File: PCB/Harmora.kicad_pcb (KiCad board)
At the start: 2 copper layers, 287 x 138 mm, 192 parts, among them J1 USBC, J4 JST-EH, J5 128x64 2.42 inc, P1 10k, P2 10k, P3 10k, P4 10k, U1 SS49E, U10 SS49E, U11 SS49E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

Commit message: vias on pads fixed
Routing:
- net GND: track 140.8 -> 135.5 mm, vias 91 -> 96
- net /MUX_S0: track 150.9 -> 149.8 mm
- net /MUX_S1: track 149.9 -> 148.8 mm
- net /MUX_S2: track 150.4 -> 149.3 mm
- net /GPIO Expanders/I2C_SDA: track 129.8 -> 129.3 mm

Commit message: finished reworking pcb
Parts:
- added R25: 10k, Footprints:0603_R, F.Cu at (196.9, 91.0)
- added R26: 10k, Footprints:0603_R, F.Cu at (185.8, 120.2)
- added R27: 10k, Footprints:0603_R, F.Cu at (176.6, 87.8)
- added R28: 10k, Footprints:0603_R, F.Cu at (176.6, 86.1)
- added R29: 10k, Footprints:0603_R, F.Cu at (165.2, 98.5)
- added R30: 10k, Footprints:0603_R, F.Cu at (168.4, 98.5)
- added R31: 10k, Footprints:0603_R, F.Cu at (166.5, 86.2)
- added R32: 10k, Footprints:0603_R, F.Cu at (166.5, 87.9)
- added R33: 10k, Footprints:0603_R, F.Cu at (118.6, 117.0)
- added R34: 10k, Footprints:0603_R, F.Cu at (118.6, 115.2)
- added R35: 10k, Footprints:0603_R, F.Cu at (138.6, 86.8)
- added R36: 10k, Footprints:0603_R, F.Cu at (138.6, 88.5)
- moved R17 23.6 mm to (182.9, 120.2), turned to -90 degrees
- moved R16 3.20 mm to (248.0, 77.3)
- moved J4 2.22 mm to (192.2, 97.5)
- moved R20 1.34 mm to (193.0, 92.0)
- moved R21 1.34 mm to (193.0, 93.5)
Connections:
- net /SOFT_SPI_CLK renamed /ATmega32u4/SPI LED chain/SOFT_SPI_CLK
- net /SOFT_SPI_MOSI renamed /ATmega32u4/SPI LED chain/SOFT_SPI_MOSI
- DM2 pad 16: (no net) -> VCC
- DM3 pad 16: (no net) -> VCC
- EX2 pad 8: DISPLAY_RST -> unconnected-(EX2-GPB7-Pad8)
- J1 pad A9: Net-(J1-VBUS) -> (no net)
- J1 pad B6: Net-(J1-D+) -> (no net)
- J1 pad B7: Net-(J1-D-) -> (no net)
- J3 pad 3: Net-(J3-MISO) -> /SPI_MISO
- J3 pad 4: Net-(J3-MOSI) -> /SPI_MOSI
- J3 pad 5: Net-(J3-SCK) -> /SPI_SCK
- J5 pad 4: /DISPLAY_DR -> /SPI_MOSI
- J5 pad 5: /SPI_MOSI -> /ATmega32u4/DISPLAY_RST
- J5 pad 6: /DISPLAY_SS -> /ATmega32u4/DISPLAY_DC
- J5 pad 7: DISPLAY_RST -> /ATmega32u4/DISPLAY_SS
- R10 pad 1: Net-(U14-(PCINT0/CLK0/ICP1)PB0) -> /ATmega32u4/SOFT_SPI_MOSI
- R11 pad 1: Net-(U14-(PCINT1/OC1A)PB1) -> /ATmega32u4/SOFT_SPI_CLK
- R16 pad 2: DISPLAY_RST -> /ATmega32u4/DISPLAY_RST
- R17 pad 1: Net-(U14-(PCINT2/~{SS}/OC1B)PB2) -> Net-(DM3-I5)
- R18 pad 2: /DISPLAY_SS -> /ATmega32u4/DISPLAY_SS
- R22 pad 2: Net-(J3-SCK) -> /SPI_SCK
- R23 pad 2: Net-(J3-MOSI) -> /SPI_MOSI
- R24 pad 2: Net-(J3-MISO) -> /SPI_MISO
- U14 pad 1: /DISPLAY_SS -> unconnected-(U14-(PCINT19/OC2B/INT1)PD3-Pad1)
- U14 pad 12: Net-(U14-(PCINT0/CLK0/ICP1)PB0) -> unconnected-(U14-(PCINT0/CLK0/ICP1)PB0-Pad12)
- U14 pad 13: Net-(U14-(PCINT1/OC1A)PB1) -> unconnected-(U14-(PCINT1/OC1A)PB1-Pad13)
- U14 pad 14: Net-(U14-(PCINT2/~{SS}/OC1B)PB2) -> /SPI_SS
- U14 pad 23: /32U4_SS -> unconnected-(U14-(ADC0/PCINT8)PC0-Pad23)
- U14 pad 30: /DISPLAY_DR -> unconnected-(U14-(RXD/PCINT16)PD0-Pad30)
- U15 pad 10: Net-(J3-MOSI) -> /SPI_MOSI
- U15 pad 11: Net-(J3-MISO) -> /SPI_MISO
- U15 pad 18: unconnected-(U15-(OC0B/SCL/INT0)PD0-Pad18) -> /SPI_SS
- U15 pad 19: unconnected-(U15-(SDA/INT1)PD1-Pad19) -> /ATmega32u4/328p_RESET
- U15 pad 20: unconnected-(U15-(RXD1/INT2)PD2-Pad20) -> /32U4_INT
- U15 pad 22: unconnected-(U15-(XCK1/~{CTS})PD5-Pad22) -> /ATmega32u4/DISPLAY_DC
- U15 pad 26: unconnected-(U15-(T1/~{OC4D}/ADC9)PD6-Pad26) -> /ATmega32u4/DISPLAY_SS
- U15 pad 27: unconnected-(U15-(T0/OC4D/ADC10)PD7-Pad27) -> /ATmega32u4/DISPLAY_RST
- U15 pad 31: /ATmega32u4/328p_RESET -> /ATmega32u4/SOFT_SPI_MOSI
- U15 pad 32: /32U4_INT -> /ATmega32u4/SOFT_SPI_CLK
- U15 pad 7: unconnected-(U15-VBUS-Pad7) -> VCC
- U15 pad 8: /32U4_SS -> Net-(U15-(SS/PCINT0)PB0)
- U15 pad 9: Net-(J3-SCK) -> /SPI_SCK
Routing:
- net VCC: track 1783.2 -> 1932.9 mm, vias 22 -> 26
- net /DISPLAY_SS: track 105.8 -> 0.00 mm, vias 2 -> 0
- net /ATmega32u4/SOFT_SPI_CLK: track 0.00 -> 97.5 mm, vias 0 -> 2
- net /ATmega32u4/SOFT_SPI_MOSI: track 0.00 -> 95.1 mm, vias 0 -> 2
- net /DISPLAY_DR: track 93.8 -> 0.00 mm
- net /SPI_SS: track 0.00 -> 71.6 mm, vias 0 -> 2
- net /32U4_SS: track 61.6 -> 0.00 mm, vias 2 -> 0
- net /ATmega32u4/DISPLAY_SS: track 0.00 -> 51.2 mm, vias 0 -> 4
- net /ATmega32u4/DISPLAY_RST: track 0.00 -> 49.5 mm, vias 0 -> 2
- net /ATmega32u4/DISPLAY_DC: track 0.00 -> 48.8 mm, vias 0 -> 2
- net DISPLAY_RST: track 44.5 -> 0.00 mm, vias 1 -> 0
- net /SPI_MOSI: track 164.1 -> 136.1 mm
- net /SPI_SCK: track 162.2 -> 135.8 mm
- net Net-(DM2-I7): track 8.94 -> 31.7 mm, vias 0 -> 1
- net Net-(J3-SCK): track 22.0 -> 0.00 mm
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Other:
- board text removed: "EFFECTS"
- board text removed: "VII"
- board text removed: "bVII"

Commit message: remane tag V2
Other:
- board text added: "HARMORA 328 V2"
- board text removed: "HARMORA 328 V1"

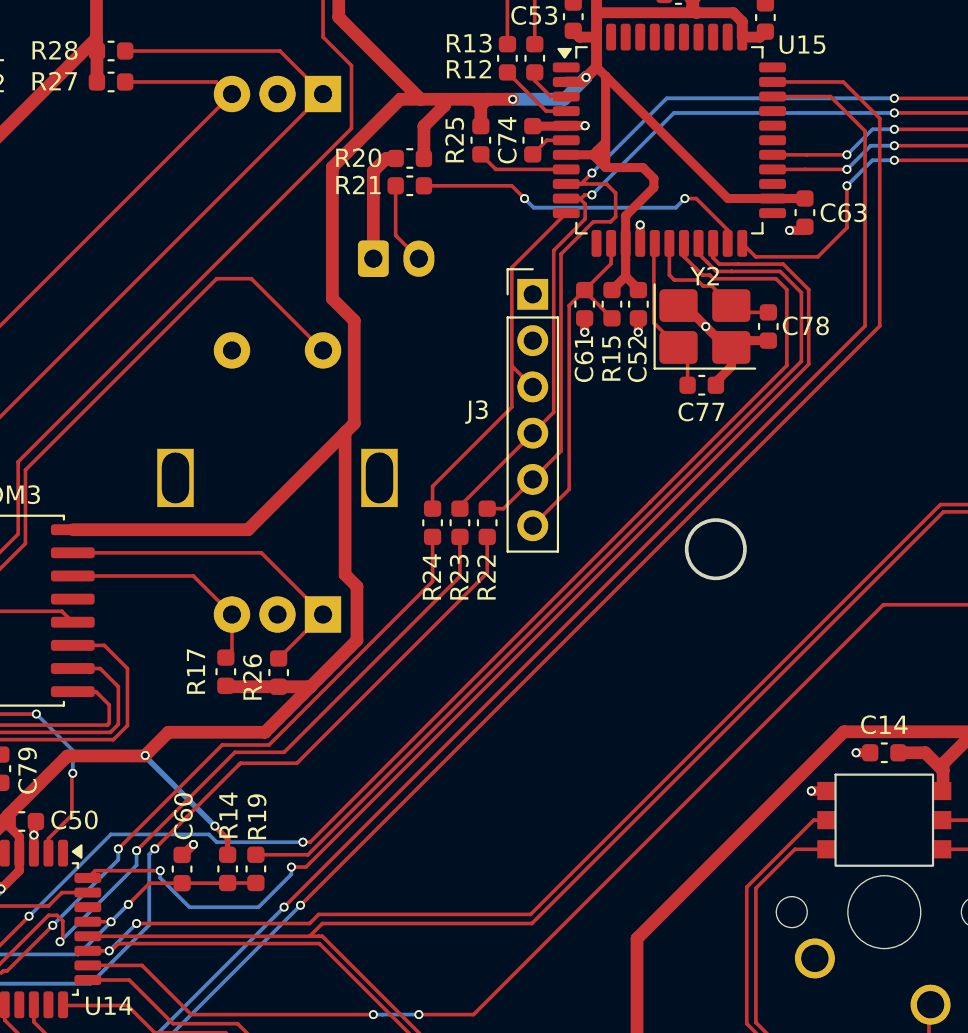
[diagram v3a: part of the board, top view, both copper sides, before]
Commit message: MCU_INT to proper pin, VCC to ISP port
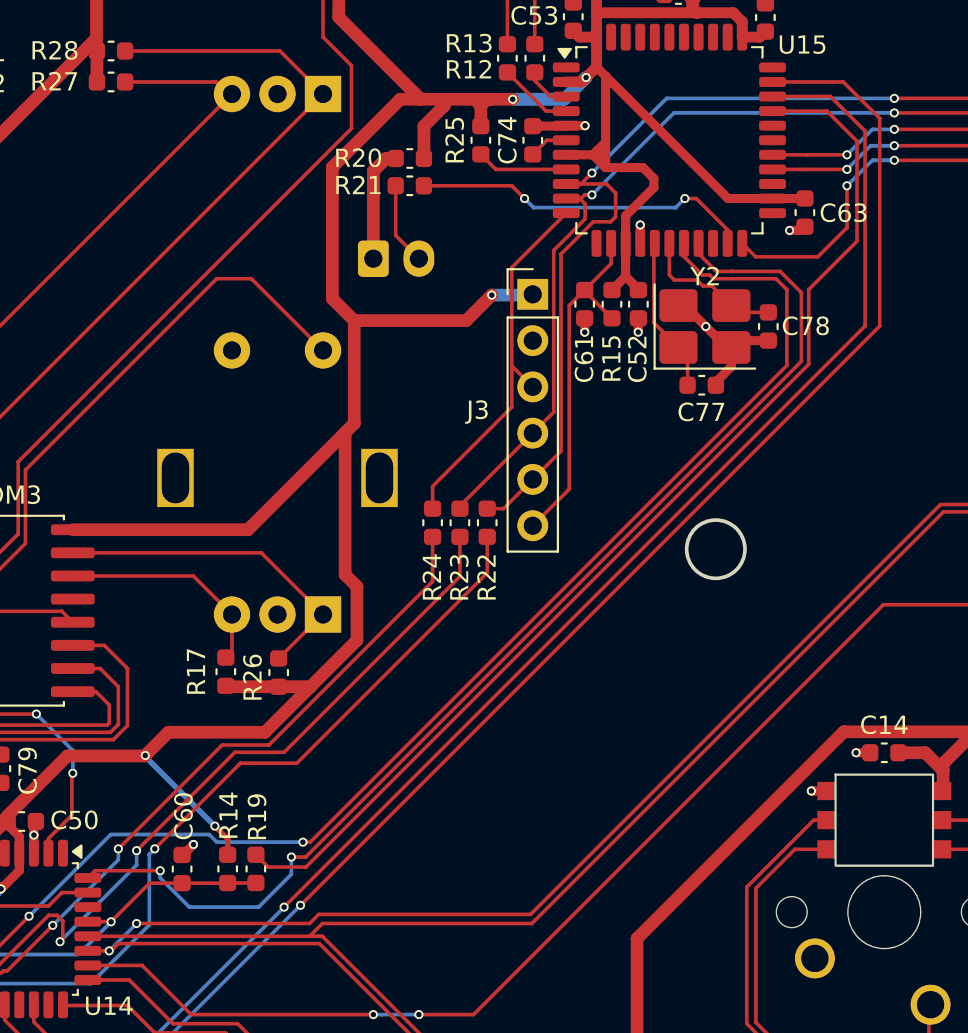
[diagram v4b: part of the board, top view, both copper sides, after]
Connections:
- J3 pad 3: /SPI_MISO -> Net-(J3-MISO)
- R24 pad 2: /SPI_MISO -> Net-(J3-MISO)
- U15 pad 11: /SPI_MISO -> Net-(J3-MISO)
- U15 pad 19: /ATmega32u4/328p_RESET -> /32U4_INT
- U15 pad 20: /32U4_INT -> (no net)
- U15 pad 30: unconnected-(U15-(PCINT6/OC1B/OC4B/ADC13)PB6-Pad30) -> /ATmega32u4/328p_RESET
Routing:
- net Net-(J3-MISO): track 0.00 -> 20.9 mm
- net /SPI_MISO: track 86.7 -> 65.8 mm
- net VCC: track 1932.9 -> 1943.3 mm, vias 26 -> 27
- net /ATmega32u4/328p_RESET: track 52.0 -> 60.7 mm
- net /RESET: vias 3 -> 2
